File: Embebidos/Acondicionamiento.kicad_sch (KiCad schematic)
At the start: 23 parts, among them IC1 ESP32-WROVER-B__8MB_, SW1 SW_Reset, SW2 SW_Boot

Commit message: fpesp
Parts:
- C1, C2, C3, C4: footprint (none) -> Capacitor_SMD:C_0805_2012Metric_Pad1.18x1.45mm_HandSolder
- D1, D2: footprint (none) -> LED_SMD:LED_0805_2012Metric_Pad1.15x1.40mm_HandSolder
- IC1: footprint ESP32WROVERB8MB -> ESP32-WROVER-B__16MB_:XCVR_ESP32-WROVER-B_(16MB)
- JP1, JP2: footprint (none) -> Connector_PinHeader_2.54mm:PinHeader_1x02_P2.54mm_Vertical
- R1, R12, R3, R6, R7: footprint (none) -> Resistor_SMD:R_0805_2012Metric_Pad1.20x1.40mm_HandSolder
- R10, R11, R2, R4, R5, R8, R9: value ~ -> 470; footprint (none) -> Resistor_SMD:R_0805_2012Metric_Pad1.20x1.40mm_HandSolder
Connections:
- net +3.3V: now also R3.2
- net RESET: now also C3.2, SW1.1 (A), SW1.2 (A)
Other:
- moved on the sheet: R3

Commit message: huellass
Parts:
- SW1, SW2: footprint (none) -> PULSADOR:pulsador
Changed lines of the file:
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@@
       (effects (font (size 1.27 1.27)) (justify right))
     )
-    (property "Footprint" "" (id 2) (at 154.94 62.23 0)
+    (property "Footprint" "PULSADOR:pulsador" (id 2) (at 154.94 62.23 0)
       (effects (font (size 1.27 1.27)) hide)
     )
@@
     (property "Reference" "SW1" (id 0) (at 83.82 92.71 0))
     (property "Value" "SW_Reset" (id 1) (at 83.82 87.63 0))
-    (property "Footprint" "" (id 2) (at 83.82 93.98 0)
+    (property "Footprint" "PULSADOR:pulsador" (id 2) (at 83.82 93.98 0)
       (effects (font (size 1.27 1.27)) hide)
     )

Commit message: Correccion Errores
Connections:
- net CtrlOnOff: now reaches IC1.14 (IO12)
- no-connect marks 20 -> 19
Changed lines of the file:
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@@
   (no_connect (at 152.4 119.38))
   (no_connect (at 152.4 106.68))
-  (no_connect (at 114.3 101.6))
   (no_connect (at 152.4 73.66))
   (no_connect (at 152.4 76.2))
@@
     (stroke (width 0) (type default) (color 0 0 0 0))
   )
+  (wire (pts (xy 105.41 101.6) (xy 114.3 101.6))
+    (stroke (width 0) (type default) (color 0 0 0 0))
+  )
   (wire (pts (xy 175.26 120.65) (xy 179.07 120.65))
     (stroke (width 0) (type default) (color 0 0 0 0))
@@
   )
   (text "Recordar: Conectar RX_CP al TX del módulo CP2104\n¿Hay problema con tener el Boot en el mismo GPIO0 que usa CP2104?"
-    (at 86.36 194.31 180)
+    (at 86.36 194.31 0)
     (effects (font (size 1.27 1.27)) (justify right bottom))
   )
@@
       (effects (font (size 1.27 1.27)) (justify right) hide)
     )
+  )
+  (global_label "CtrlOnOff" (shape input) (at 105.41 101.6 180) (fields_autoplaced)
+    (effects (font (size 1.27 1.27)) (justify right))
+    (property "Intersheet References" "${INTERSHEET_REFS}" (id 0) (at 94.2883 101.5206 0)
+      (effects (font (size 1.27 1.27)) (justify right) hide)
+    )

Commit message: arreglos
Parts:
- IC1: footprint ESP32-WROVER-B__16MB_:XCVR_ESP32-WROVER-B_(16MB) -> esp32:ESP32WROVERB8MB
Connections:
- net CtrlOnOff: no longer names the net of IC1.14 (IO12)
- no-connect marks 19 -> 20
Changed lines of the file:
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@@
   (no_connect (at 152.4 119.38))
   (no_connect (at 152.4 106.68))
+  (no_connect (at 114.3 101.6))
   (no_connect (at 152.4 73.66))
   (no_connect (at 152.4 76.2))
@@
     (stroke (width 0) (type default) (color 0 0 0 0))
   )
-  (wire (pts (xy 105.41 101.6) (xy 114.3 101.6))
-    (stroke (width 0) (type default) (color 0 0 0 0))
-  )
   (wire (pts (xy 175.26 120.65) (xy 179.07 120.65))
     (stroke (width 0) (type default) (color 0 0 0 0))
@@
     )
   )
-  (global_label "CtrlOnOff" (shape input) (at 105.41 101.6 180) (fields_autoplaced)
-    (effects (font (size 1.27 1.27)) (justify right))
-    (property "Intersheet References" "${INTERSHEET_REFS}" (id 0) (at 94.2883 101.5206 0)
-      (effects (font (size 1.27 1.27)) (justify right) hide)
-    )
-  )
   (hierarchical_label "SDA_PAN" (shape input) (at 181.61 88.9 0)
     (effects (font (size 1.27 1.27)) (justify left))
@@
     (property "Reference" "IC1" (id 0) (at 133.35 60.96 0))
     (property "Value" "ESP32-WROVER-B__8MB_" (id 1) (at 133.35 63.5 0))
-    (property "Footprint" "ESP32-WROVER-B__16MB_:XCVR_ESP32-WROVER-B_(16MB)" (id 2) (at 148.59 66.04 0)
+    (property "Footprint" "esp32:ESP32WROVERB8MB" (id 2) (at 148.59 66.04 0)
       (effects (font (size 1.27 1.27)) (justify left) hide)
     )

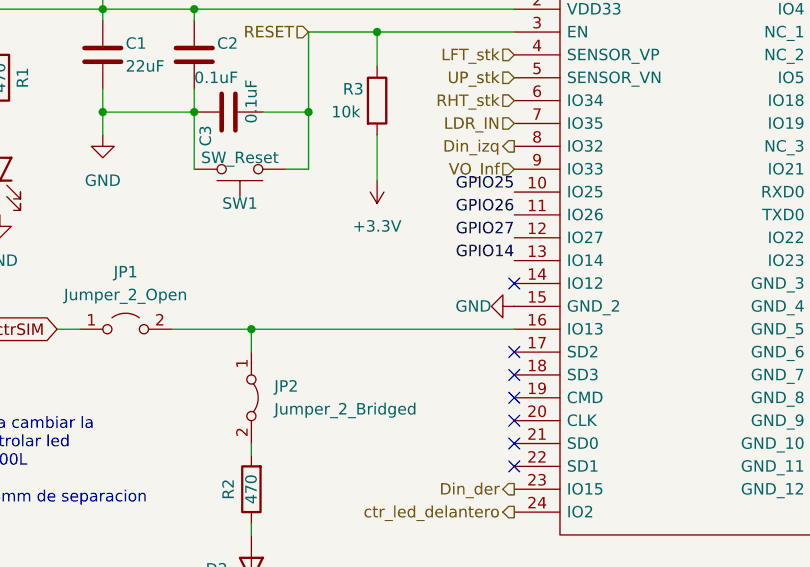
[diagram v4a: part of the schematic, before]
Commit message: Correccion errores y huellas leds LDR
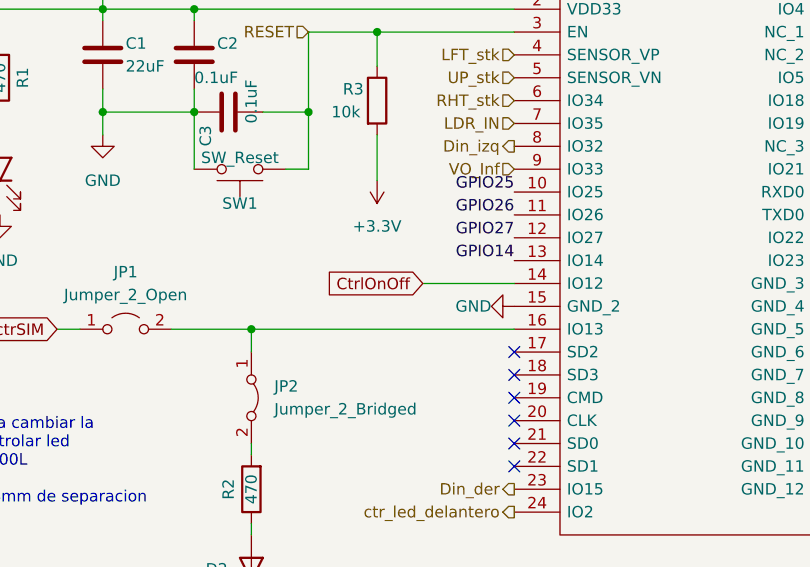
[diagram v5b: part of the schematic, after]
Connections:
- net CtrlOnOff: now reaches IC1.14 (IO12)
- no-connect marks 20 -> 19
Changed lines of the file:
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@@
   (no_connect (at 152.4 119.38))
   (no_connect (at 152.4 106.68))
-  (no_connect (at 114.3 101.6))
   (no_connect (at 152.4 73.66))
   (no_connect (at 152.4 76.2))
@@
     (stroke (width 0) (type default) (color 0 0 0 0))
   )
+  (wire (pts (xy 104.14 101.6) (xy 114.3 101.6))
+    (stroke (width 0) (type default) (color 0 0 0 0))
+  )
   (wire (pts (xy 63.5 106.68) (xy 66.04 106.68))
     (stroke (width 0) (type default) (color 0 0 0 0))
@@
     (effects (font (size 1.27 1.27)) (justify right bottom))
   )
+  (global_label "CtrlOnOff" (shape input) (at 104.14 101.6 180) (fields_autoplaced)
+    (effects (font (size 1.27 1.27)) (justify right))
+    (property "Intersheet References" "${INTERSHEET_REFS}" (id 0) (at 93.0183 101.5206 0)
+      (effects (font (size 1.27 1.27)) (justify right) hide)
+    )
+  )
   (global_label "ctrSIM" (shape input) (at 63.5 106.68 180) (fields_autoplaced)
